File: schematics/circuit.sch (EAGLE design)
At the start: 13 parts, among them U1 AD5241BRU1M-REEL7AD5241BRZ1M, U3 ADXL375BCCZ, X1 87758-1816

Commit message: Обновленная версия схемы
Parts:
- added R1, R2, R4, R5: (no value), rcl:R-US_0207/10
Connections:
- new net N$3: R4.2, U1.SCL, X1-7.S
- new net N$5: R5.2, U1.SDA, X1-9.S
- new net N$7: R2.2, U3.SCL/SCLK, X1-4.S
- new net N$8: R1.2, U3.SDA/SDI/SDIO, X1-6.S
- net 3.3V: now also R2.1, U3.*CS, U3.RESERVED, U3.SDO/ALT_ADDRESS
- net GND: now also R4.1, R5.1, U1.DGND
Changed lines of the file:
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@@
 <part name="U3" library="elements" deviceset="ADXL375BCCZ" device=""/>
 <part name="GND4" library="SparkFun-Aesthetics" deviceset="GND" device=""/>
+<part name="R4" library="rcl" deviceset="R-US_" device="0207/10"/>
+<part name="R5" library="rcl" deviceset="R-US_" device="0207/10"/>
+<part name="R1" library="rcl" deviceset="R-US_" device="0207/10"/>
+<part name="R2" library="rcl" deviceset="R-US_" device="0207/10"/>
+<part name="GND5" library="supply1" deviceset="GND" device=""/>
 </parts>
 <sheets>
@@
 <instance part="U3" gate="A" x="93.98" y="22.86"/>
 <instance part="GND4" gate="1" x="134.62" y="22.86"/>
+<instance part="R4" gate="G$1" x="-10.16" y="12.7"/>
+<instance part="R5" gate="G$1" x="-17.78" y="-2.54"/>
+<instance part="R1" gate="G$1" x="40.64" y="20.32"/>
+<instance part="R2" gate="G$1" x="45.72" y="25.4"/>
+<instance part="GND5" gate="1" x="55.88" y="-27.94"/>
 </instances>
 <busses>
@@
 <wire x1="63.5" y1="0" x2="124.46" y2="0" width="0.1524" layer="91"/>
 <pinref part="U3" gate="A" pin="RESERVED_2"/>
-<wire x1="124.46" y1="0" x2="124.46" y2="17.78" width="0.1524" layer="91"/>
+<wire x1="124.46" y1="0" x2="124.46" y2="15.24" width="0.1524" layer="91"/>
+<wire x1="124.46" y1="15.24" x2="124.46" y2="17.78" width="0.1524" layer="91"/>
 <wire x1="124.46" y1="17.78" x2="121.92" y2="17.78" width="0.1524" layer="91"/>
 <pinref part="U3" gate="A" pin="VDD_I/O"/>
@@
 <junction x="63.5" y="35.56"/>
 <wire x1="33.02" y1="76.2" x2="33.02" y2="35.56" width="0.1524" layer="91"/>
-<wire x1="33.02" y1="35.56" x2="63.5" y2="35.56" width="0.1524" layer="91"/>
+<wire x1="33.02" y1="35.56" x2="38.1" y2="35.56" width="0.1524" layer="91"/>
 <junction x="33.02" y="76.2"/>
+<pinref part="U3" gate="A" pin="RESERVED"/>
+<wire x1="38.1" y1="35.56" x2="60.96" y2="35.56" width="0.1524" layer="91"/>
+<wire x1="60.96" y1="35.56" x2="63.5" y2="35.56" width="0.1524" layer="91"/>
+<wire x1="121.92" y1="15.24" x2="124.46" y2="15.24" width="0.1524" layer="91"/>
+<junction x="124.46" y="15.24"/>
+<pinref part="U3" gate="A" pin="*CS"/>
+<wire x1="66.04" y1="10.16" x2="60.96" y2="10.16" width="0.1524" layer="91"/>
+<wire x1="60.96" y1="10.16" x2="60.96" y2="15.24" width="0.1524" layer="91"/>
+<junction x="60.96" y="35.56"/>
+<pinref part="U3" gate="A" pin="SDO/ALT_ADDRESS"/>
+<wire x1="60.96" y1="15.24" x2="60.96" y2="35.56" width="0.1524" layer="91"/>
+<wire x1="66.04" y1="15.24" x2="60.96" y2="15.24" width="0.1524" layer="91"/>
+<junction x="60.96" y="15.24"/>
+<wire x1="33.02" y1="35.56" x2="33.02" y2="20.32" width="0.1524" layer="91"/>
+<junction x="33.02" y="35.56"/>
+<wire x1="33.02" y1="20.32" x2="38.1" y2="20.32" width="0.1524" layer="91"/>
+<wire x1="38.1" y1="35.56" x2="38.1" y2="25.4" width="0.1524" layer="91"/>
+<junction x="38.1" y="35.56"/>
+<pinref part="R2" gate="G$1" pin="1"/>
+<wire x1="38.1" y1="25.4" x2="40.64" y2="25.4" width="0.1524" layer="91"/>
 </segment>
 </net>
@@
 <junction x="-12.7" y="40.64"/>
 <wire x1="10.16" y1="5.08" x2="2.54" y2="5.08" width="0.1524" layer="91"/>
-<wire x1="2.54" y1="5.08" x2="-27.94" y2="5.08" width="0.1524" layer="91"/>
+<wire x1="2.54" y1="5.08" x2="-17.78" y2="5.08" width="0.1524" layer="91"/>
+<wire x1="-17.78" y1="5.08" x2="-27.94" y2="5.08" width="0.1524" layer="91"/>
 <wire x1="-27.94" y1="5.08" x2="-27.94" y2="40.64" width="0.1524" layer="91"/>
 <junction x="-27.94" y="40.64"/>
@@
 <wire x1="2.54" y1="-25.4" x2="2.54" y2="5.08" width="0.1524" layer="91"/>
 <junction x="2.54" y="5.08"/>
+<pinref part="R4" gate="G$1" pin="1"/>
+<wire x1="-15.24" y1="12.7" x2="-17.78" y2="12.7" width="0.1524" layer="91"/>
+<wire x1="-17.78" y1="12.7" x2="-17.78" y2="5.08" width="0.1524" layer="91"/>
+<junction x="-17.78" y="5.08"/>
+<wire x1="-27.94" y1="5.08" x2="-27.94" y2="-2.54" width="0.1524" layer="91"/>
+<junction x="-27.94" y="5.08"/>
+<pinref part="R5" gate="G$1" pin="1"/>
+<wire x1="-27.94" y1="-2.54" x2="-22.86" y2="-2.54" width="0.1524" layer="91"/>
 </segment>
 <segment>
@@
 <junction x="127" y="25.4"/>
 <pinref part="GND4" gate="1" pin="GND"/>
+</segment>
+<segment>
+<pinref part="U1" gate="A" pin="DGND"/>
+<wire x1="45.72" y1="-22.86" x2="55.88" y2="-22.86" width="0.1524" layer="91"/>
+<wire x1="55.88" y1="-22.86" x2="55.88" y2="-25.4" width="0.1524" layer="91"/>
+<pinref part="GND5" gate="1" pin="GND"/>
 </segment>
 </net>
@@
 </segment>
 </net>
+<net name="N$3" class="0">
+<segment>
+<pinref part="U1" gate="A" pin="SCL"/>
+<wire x1="10.16" y1="7.62" x2="-2.54" y2="7.62" width="0.1524" layer="91"/>
+<wire x1="-2.54" y1="7.62" x2="-38.1" y2="7.62" width="0.1524" layer="91"/>
+<wire x1="-38.1" y1="7.62" x2="-38.1" y2="111.76" width="0.1524" layer="91"/>
+<pinref part="X1" gate="-7" pin="S"/>
+<wire x1="-38.1" y1="111.76" x2="50.8" y2="111.76" width="0.1524" layer="91"/>
+<pinref part="R4" gate="G$1" pin="2"/>
+<wire x1="-5.08" y1="12.7" x2="-2.54" y2="12.7" width="0.1524" layer="91"/>
+<wire x1="-2.54" y1="12.7" x2="-2.54" y2="7.62" width="0.1524" layer="91"/>
+<junction x="-2.54" y="7.62"/>
+</segment>
+</net>
+<net name="N$5" class="0">
+<segment>
+<pinref part="X1" gate="-9" pin="S"/>
+<wire x1="50.8" y1="109.22" x2="-40.64" y2="109.22" width="0.1524" layer="91"/>
+<wire x1="-40.64" y1="109.22" x2="-40.64" y2="2.54" width="0.1524" layer="91"/>
+<pinref part="U1" gate="A" pin="SDA"/>
+<wire x1="-40.64" y1="2.54" x2="-7.62" y2="2.54" width="0.1524" layer="91"/>
+<pinref part="R5" gate="G$1" pin="2"/>
+<wire x1="-7.62" y1="2.54" x2="10.16" y2="2.54" width="0.1524" layer="91"/>
+<wire x1="-12.7" y1="-2.54" x2="-7.62" y2="-2.54" width="0.1524" layer="91"/>
+<wire x1="-7.62" y1="-2.54" x2="-7.62" y2="2.54" width="0.1524" layer="91"/>
+<junction x="-7.62" y="2.54"/>
+</segment>
+</net>
+<net name="N$7" class="0">
+<segment>
+<pinref part="X1" gate="-4" pin="S"/>
+<wire x1="137.16" y1="116.84" x2="121.92" y2="116.84" width="0.1524" layer="91"/>
+<wire x1="121.92" y1="116.84" x2="121.92" y2="55.88" width="0.1524" layer="91"/>
+<wire x1="121.92" y1="55.88" x2="68.58" y2="55.88" width="0.1524" layer="91"/>
+<wire x1="68.58" y1="55.88" x2="68.58" y2="48.26" width="0.1524" layer="91"/>
+<wire x1="68.58" y1="48.26" x2="55.88" y2="48.26" width="0.1524" layer="91"/>
+<wire x1="55.88" y1="48.26" x2="55.88" y2="25.4" width="0.1524" layer="91"/>
+<pinref part="U3" gate="A" pin="SCL/SCLK"/>
+<wire x1="55.88" y1="25.4" x2="66.04" y2="25.4" width="0.1524" layer="91"/>
+<pinref part="R2" gate="G$1" pin="2"/>
+<wire x1="50.8" y1="25.4" x2="55.88" y2="25.4" width="0.1524" layer="91"/>
+<junction x="55.88" y="25.4"/>
+</segment>
+</net>
+<net name="N$8" class="0">
+<segment>
+<pinref part="X1" gate="-6" pin="S"/>
+<wire x1="137.16" y1="114.3" x2="124.46" y2="114.3" width="0.1524" layer="91"/>
+<wire x1="124.46" y1="114.3" x2="124.46" y2="53.34" width="0.1524" layer="91"/>
+<wire x1="124.46" y1="53.34" x2="71.12" y2="53.34" width="0.1524" layer="91"/>
+<wire x1="71.12" y1="53.34" x2="71.12" y2="45.72" width="0.1524" layer="91"/>
+<wire x1="71.12" y1="45.72" x2="53.34" y2="45.72" width="0.1524" layer="91"/>
+<wire x1="53.34" y1="45.72" x2="53.34" y2="20.32" width="0.1524" layer="91"/>
+<pinref part="U3" gate="A" pin="SDA/SDI/SDIO"/>
+<wire x1="53.34" y1="20.32" x2="66.04" y2="20.32" width="0.1524" layer="91"/>
+<pinref part="R1" gate="G$1" pin="2"/>
+<wire x1="45.72" y1="20.32" x2="53.34" y2="20.32" width="0.1524" layer="91"/>
+<junction x="53.34" y="20.32"/>
+</segment>
+</net>

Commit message: исправлена схема
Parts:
- removed C2: 4.7pF, SparkFun-Capacitors:4.7PF-50V(-/+.25PF)(0603)
- removed R5: (no value), rcl:R-US_0207/10
- added R3: (no value), SparkFun-Passives:RESISTOR0402-RES
- added U$1, U$3: N-CHANNEL-MOSFET-BSS138, GeekAmmo:N-CHANNEL-MOSFET-BSS138
- R1, R2, R4: device rcl:R-US_0207/10 -> SparkFun-Passives:RESISTOR0402-RES
- renumbered U1 to DP, U3 to ACC
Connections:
- removed net N$3: DP.SCL, R4.2, X1-7.S
- removed net N$5: DP.SDA, R5.2, X1-9.S
- removed net N$7: ACC.SCL/SCLK, R2.2, X1-4.S
- removed net N$8: ACC.SDA/SDI/SDIO, R1.2, X1-6.S
- new net SCL3.3V: ACC.SCL/SCLK, DP.SCL, R2.1, U$3.S
- new net SCL5V: R1.1, U$3.D, X1-6.S
- new net SDA3.3V: ACC.SDA/SDI/SDIO, DP.SDA, R3.1, U$1.S
- new net SDA5V: R4.1, U$1.D, X1-4.S
- new net VCC: DP.SHDN*, DP.VDD
- net 3.3V: now also R2.2, R3.2, U$1.G, U$3.G; no longer R2.1
- net 5V: now also R1.2, R4.2
- net GND: no longer C2.2, C4.2, DP.SHDN*, DP.VDD, R4.1, R5.1
- net VBAT: now also C4.2; no longer C2.1
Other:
- note added: "3.3V"
- note added: "5V"
- note added: "SCL"
- note added: "SDA"
- moved on the sheet: C4, R1, R2, R4

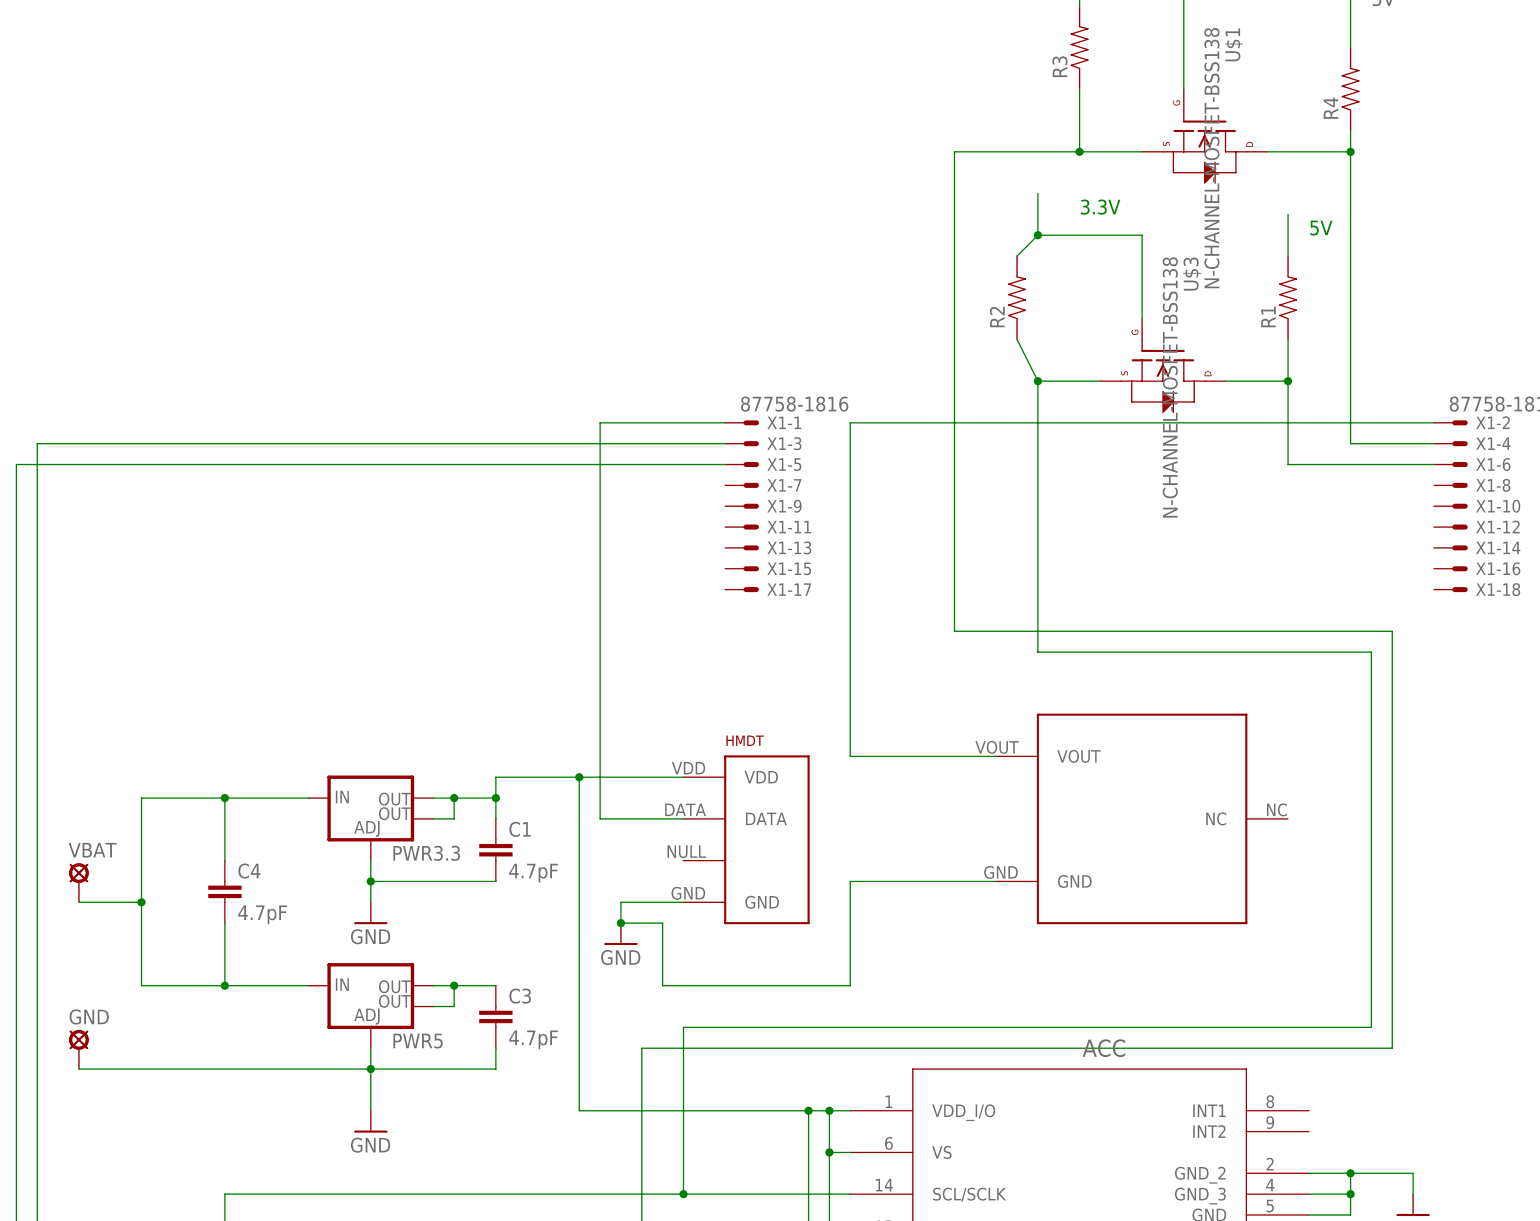
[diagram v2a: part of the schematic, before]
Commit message: [схемы] удалил лишнее и переместил на место то, что сбежало
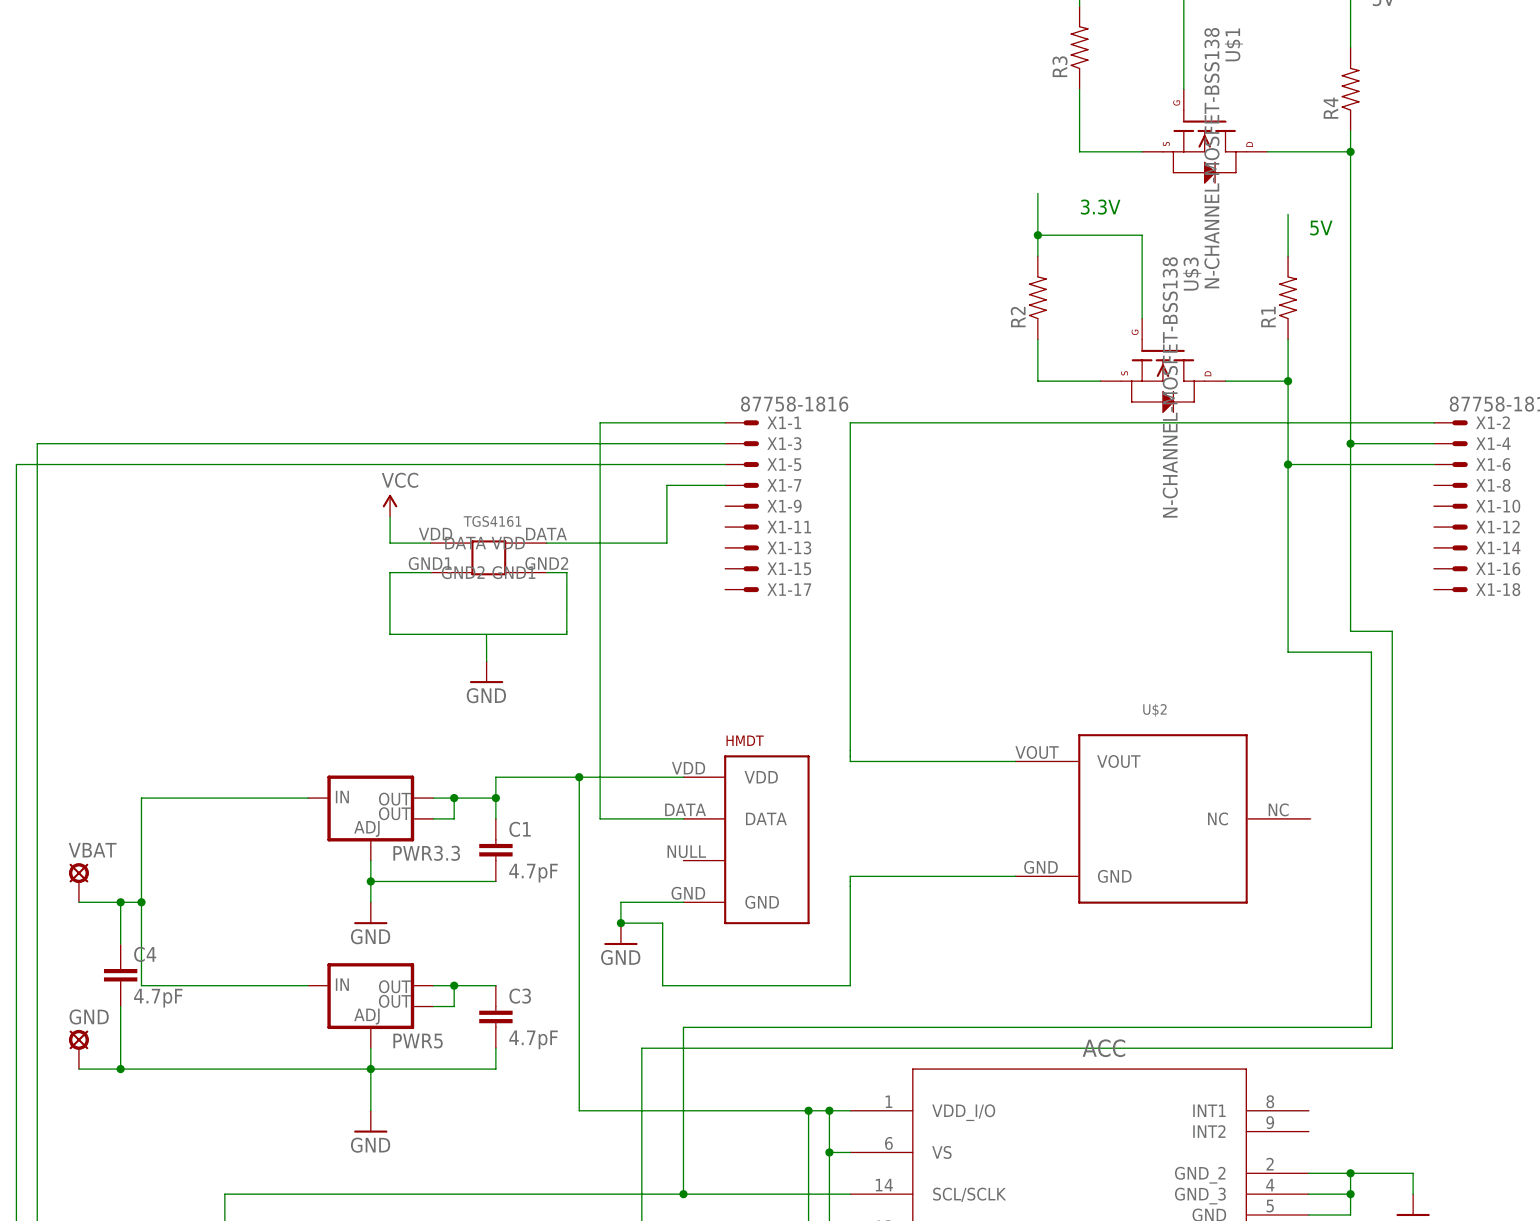
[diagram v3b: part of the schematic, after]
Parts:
- added TGS4161: TGS4161, opt3001:TGS4161
- U$2: value SK25F -> O2-A2; device sk25f:SK25F -> opt3001:O2-A2
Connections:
- removed net SCL3.3V: ACC.SCL/SCLK, DP.SCL, R2.1, U$3.S
- removed net SDA3.3V: ACC.SDA/SDI/SDIO, DP.SDA, R3.1, U$1.S
- removed net VCC: DP.SHDN*, DP.VDD
- new net N$3: R3.1, U$1.S
- new net N$5: R2.1, U$3.S
- net 5V: now also DP.SHDN*, DP.VDD
- net GND: now also C4.2; no longer U$2.GND
- net N$1: no longer U$2.VOUT
- net SCL5V: now also ACC.SCL/SCLK, DP.SCL
- net SDA5V: now also ACC.SDA/SDI/SDIO, DP.SDA
- net VBAT: no longer C4.2
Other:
- moved on the sheet: C4, R2
